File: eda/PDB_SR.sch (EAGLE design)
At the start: 14 parts

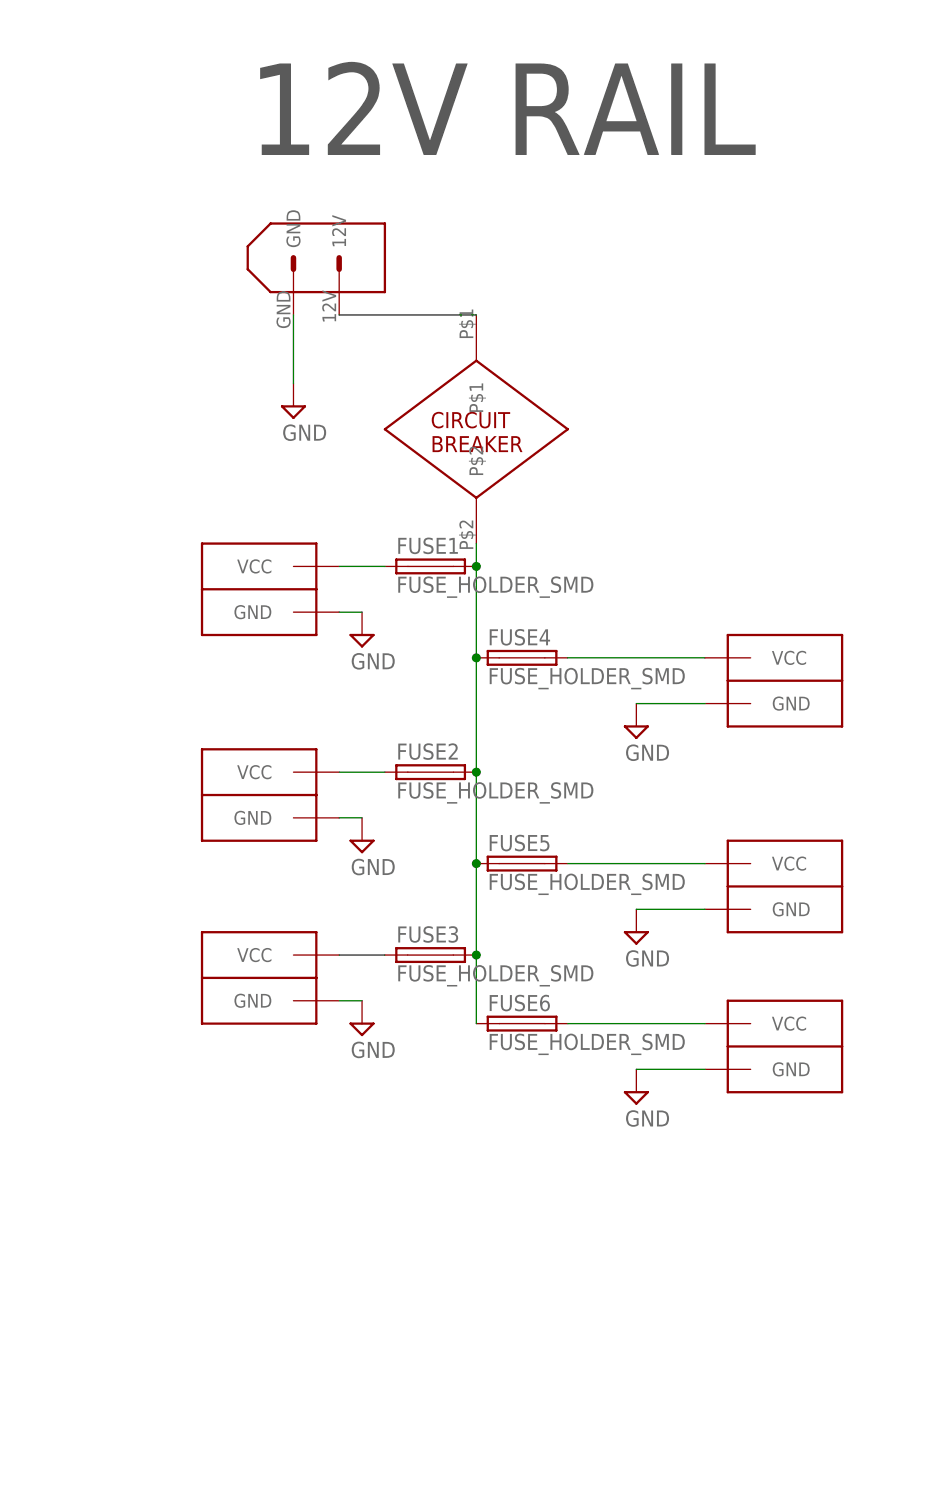
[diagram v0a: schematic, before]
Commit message: Revert "Updated PDB Design"
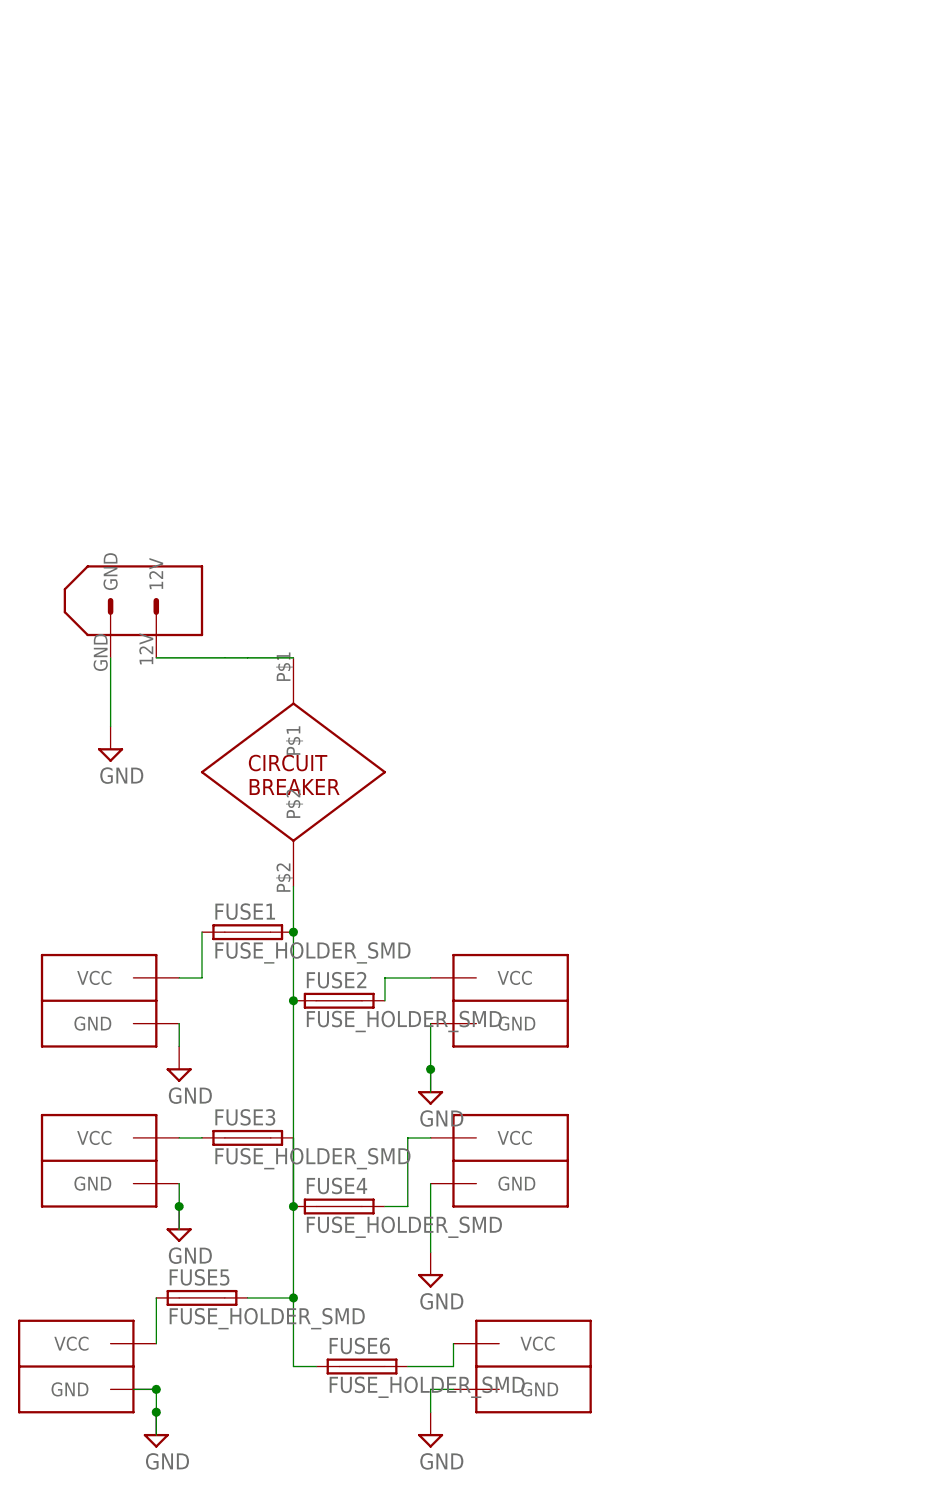
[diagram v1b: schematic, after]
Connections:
- net 12V: now also FUSE2.1, FUSE5.2; no longer FUSE2.2, FUSE5.1
- net VOUT1: now also CONN2.VCC; no longer CONN1.VCC
- net VOUT2: now also CONN4.VCC, FUSE2.2; no longer CONN2.VCC, FUSE2.1
- net VOUT3: now also CONN1.VCC; no longer CONN3.VCC
- net VOUT4: now also CONN5.VCC; no longer CONN4.VCC
- net VOUT5: now also CONN3.VCC, FUSE5.1; no longer CONN5.VCC, FUSE5.2
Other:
- note removed: "12V RAIL"
- moved on the sheet: FUSE1, FUSE2, FUSE3, FUSE4, FUSE5, FUSE6
